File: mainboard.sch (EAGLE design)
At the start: 128 parts, among them X1 FH12-24S-0.5SH, X3 87438-02

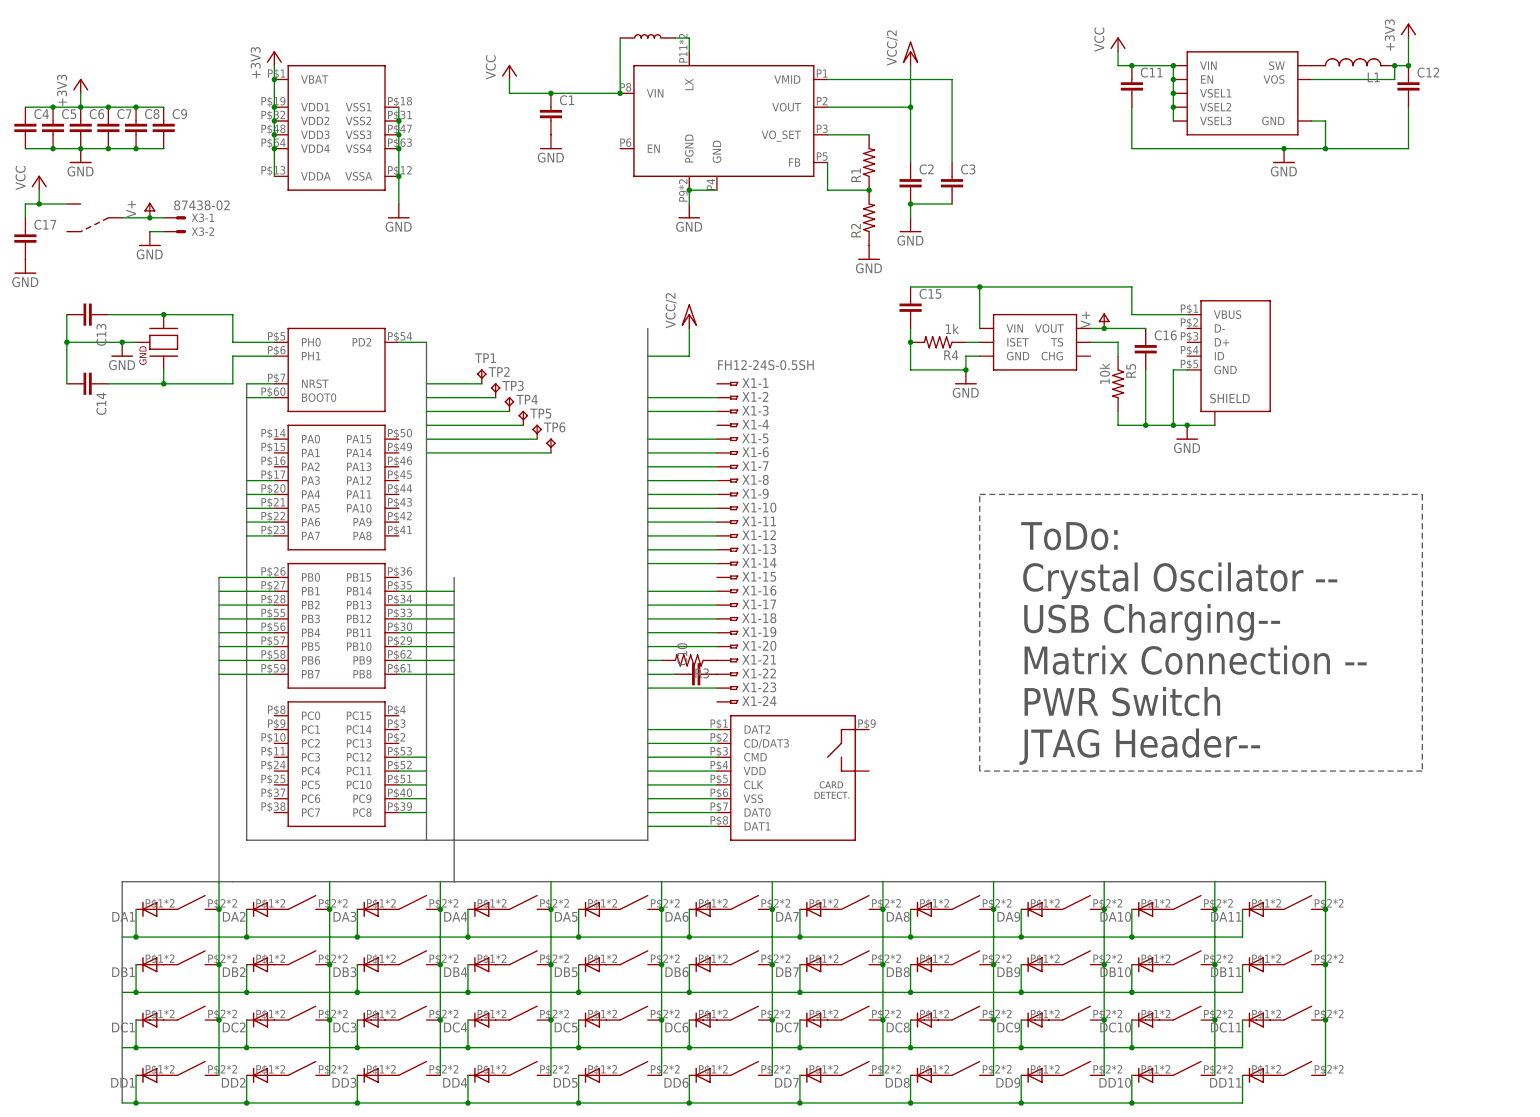
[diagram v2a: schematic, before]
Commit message: Fixed Issues/New features
Battery level sensing
microSD card sensing

Fixed issues:
Boot0 pulldown resistor
NRST pullup resistor
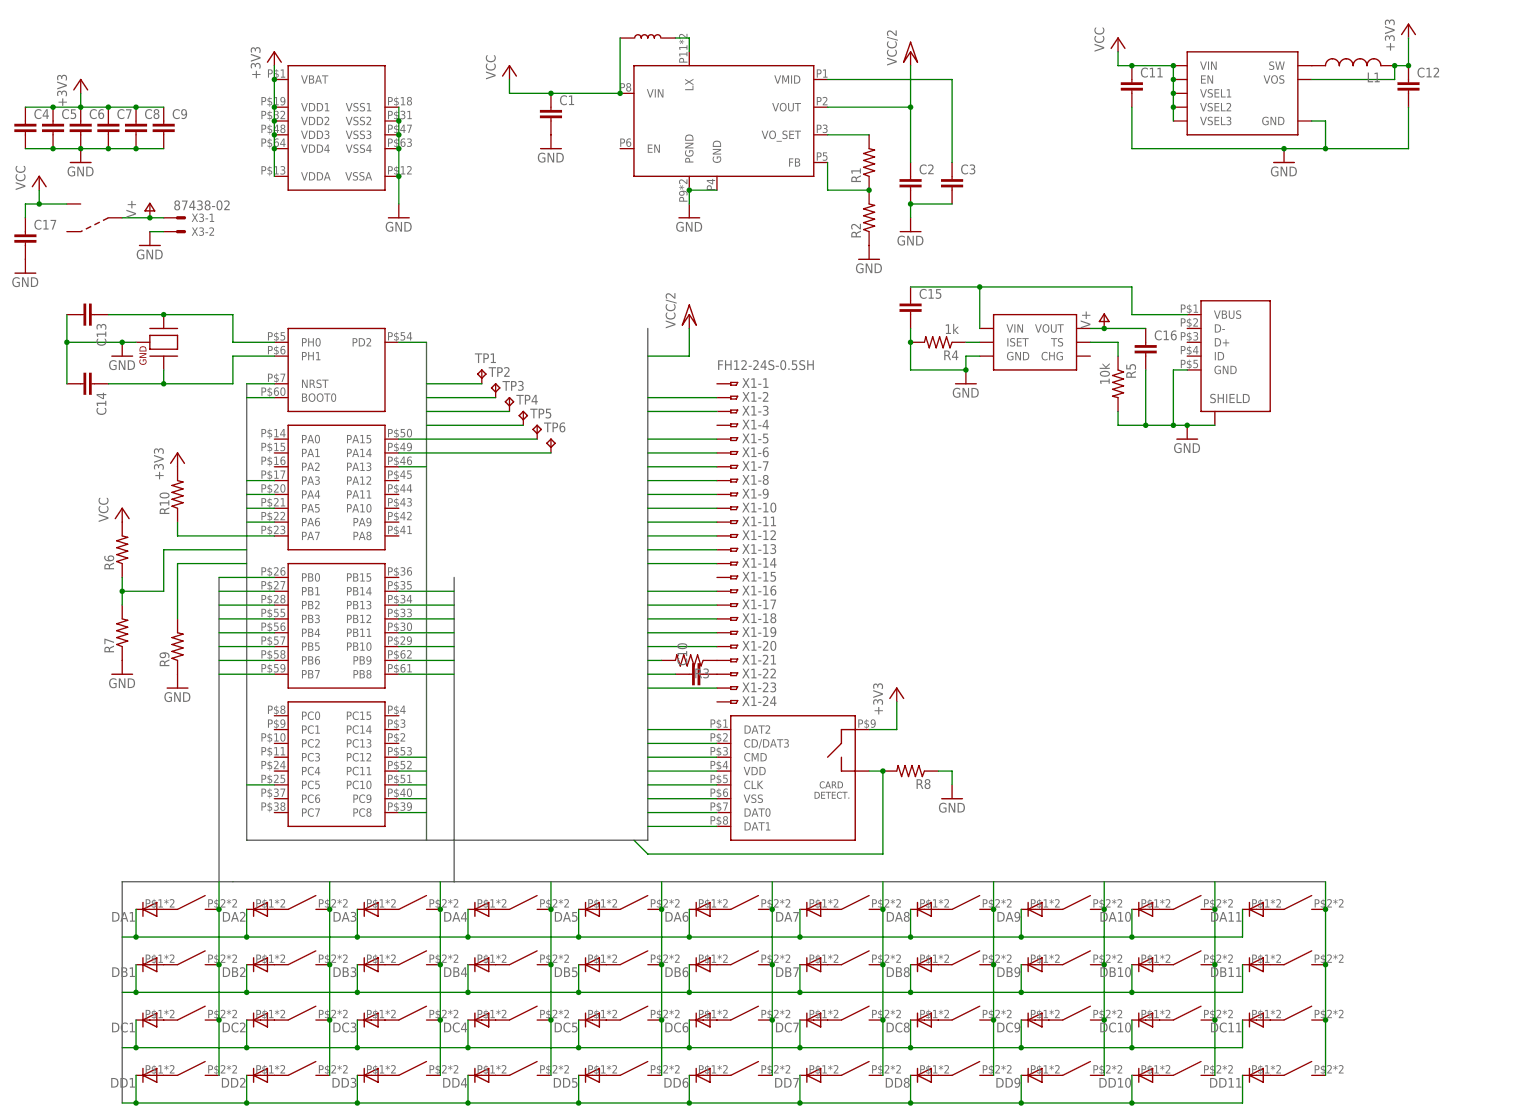
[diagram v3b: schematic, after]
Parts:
- added R10, R6, R7, R8, R9: (no value), resistor:R-US_R0402
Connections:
- new net BAT_SENS: R6.1, R7.2, U$1G$4.PC5
- new net SD_SWITCH: R8.2, U$1G$2.PA15, U$2.P$10
- net +3V3: now also R10.2, U$2.P$9
- net BOOT0: now also R9.2
- net GND: now also R7.1, R8.1, R9.1
- net NRST: now also R10.1
- net PA13: now also U$1G$2.PA13
- net PA14: now also U$1G$2.PA14
- net VCC: now also R6.2
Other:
- note removed: "ToDo: Crystal Oscilator -- USB Charging-- Matrix Connection -- PWR Switch JTAG Header--"
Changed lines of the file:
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@@
 <part name="C17" library="eagle-ltspice" deviceset="C" device="C1206"/>
 <part name="GND12" library="supply1" deviceset="GND" device=""/>
+<part name="R6" library="resistor" deviceset="R-US_" device="R0402"/>
+<part name="R7" library="resistor" deviceset="R-US_" device="R0402"/>
+<part name="GND13" library="supply1" deviceset="GND" device=""/>
+<part name="P+6" library="supply1" deviceset="VCC" device=""/>
+<part name="+3V4" library="supply1" deviceset="+3V3" device=""/>
+<part name="R8" library="resistor" deviceset="R-US_" device="R0402"/>
+<part name="GND14" library="supply1" deviceset="GND" device=""/>
+<part name="R9" library="resistor" deviceset="R-US_" device="R0402"/>
+<part name="GND15" library="supply1" deviceset="GND" device=""/>
+<part name="R10" library="resistor" deviceset="R-US_" device="R0402"/>
+<part name="+3V5" library="supply1" deviceset="+3V3" device=""/>
 </parts>
 <sheets>
 <sheet>
 <plain>
-<text x="170.18" y="66.04" size="5.08" layer="97">ToDo:
-Crystal Oscilator --
-USB Charging--
-Matrix Connection --
-PWR Switch
-JTAG Header--</text>
-<wire x1="162.56" y1="114.3" x2="243.84" y2="114.3" width="0.1524" layer="97" style="shortdash"/>
-<wire x1="243.84" y1="114.3" x2="243.84" y2="63.5" width="0.1524" layer="97" style="shortdash"/>
-<wire x1="243.84" y1="63.5" x2="162.56" y2="63.5" width="0.1524" layer="97" style="shortdash"/>
-<wire x1="162.56" y1="63.5" x2="162.56" y2="114.3" width="0.1524" layer="97" style="shortdash"/>
 </plain>
 <instances>
@@
 <instance part="C17" gate="G$1" x="-12.7" y="162.56"/>
 <instance part="GND12" gate="1" x="-12.7" y="154.94"/>
+<instance part="R6" gate="G$1" x="5.08" y="104.14" rot="R90"/>
+<instance part="R7" gate="G$1" x="5.08" y="88.9" rot="R90"/>
+<instance part="GND13" gate="1" x="5.08" y="81.28"/>
+<instance part="P+6" gate="VCC" x="5.08" y="111.76"/>
+<instance part="+3V4" gate="G$1" x="147.32" y="78.74"/>
+<instance part="R8" gate="G$1" x="149.86" y="63.5" rot="R180"/>
+<instance part="GND14" gate="1" x="157.48" y="58.42"/>
+<instance part="R9" gate="G$1" x="15.24" y="86.36" rot="R90"/>
+<instance part="GND15" gate="1" x="15.24" y="78.74"/>
+<instance part="R10" gate="G$1" x="15.24" y="114.3" rot="R90"/>
+<instance part="+3V5" gate="G$1" x="15.24" y="121.92"/>
 </instances>
 <busses>
-<bus name="SD_CLK,SD_CMD,SD_DAT[0..3],+3V3,GND,SPI_CS,SPI_SCK,SPI_MISO,SPI_MOSI,VCC/2,PA[0..15],PB[0..15],PC[0..15],BOOT0,NRST">
+<bus name="SD_CLK,SD_CMD,SD_DAT[0..3],+3V3,GND,SPI_CS,SPI_SCK,SPI_MISO,SPI_MOSI,VCC/2,PA[0..15],PB[0..15],PC[0..15],BOOT0,NRST,BAT_SENS,SD_SWITCH">
 <segment>
 <wire x1="27.94" y1="134.62" x2="27.94" y2="50.8" width="0.762" layer="92"/>
@@
 <pinref part="C17" gate="G$1" pin="2"/>
 <pinref part="GND12" gate="1" pin="GND"/>
+</segment>
+<segment>
+<pinref part="R7" gate="G$1" pin="1"/>
+<pinref part="GND13" gate="1" pin="GND"/>
+</segment>
+<segment>
+<pinref part="R8" gate="G$1" pin="1"/>
+<pinref part="GND14" gate="1" pin="GND"/>
+<wire x1="154.94" y1="63.5" x2="157.48" y2="63.5" width="0.1524" layer="91"/>
+<wire x1="157.48" y1="63.5" x2="157.48" y2="60.96" width="0.1524" layer="91"/>
+</segment>
+<segment>
+<pinref part="R9" gate="G$1" pin="1"/>
+<pinref part="GND15" gate="1" pin="GND"/>
 </segment>
 </net>
@@
 <pinref part="TP1" gate="G$1" pin="TP"/>
 <wire x1="71.12" y1="134.62" x2="60.96" y2="134.62" width="0.1524" layer="91"/>
+</segment>
+<segment>
+<pinref part="U$2" gate="G$1" pin="P$9"/>
+<pinref part="+3V4" gate="G$1" pin="+3V3"/>
+<wire x1="142.24" y1="71.12" x2="147.32" y2="71.12" width="0.1524" layer="91"/>
+<wire x1="147.32" y1="71.12" x2="147.32" y2="76.2" width="0.1524" layer="91"/>
+</segment>
+<segment>
+<pinref part="R10" gate="G$1" pin="2"/>
+<pinref part="+3V5" gate="G$1" pin="+3V3"/>
 </segment>
 </net>
@@
 <wire x1="-10.16" y1="167.64" x2="-5.08" y2="167.64" width="0.1524" layer="91"/>
 <junction x="-10.16" y="167.64"/>
+</segment>
+<segment>
+<pinref part="R6" gate="G$1" pin="2"/>
+<pinref part="P+6" gate="VCC" pin="VCC"/>
 </segment>
 </net>
@@
 <wire x1="73.66" y1="132.08" x2="60.96" y2="132.08" width="0.1524" layer="91"/>
 </segment>
+<segment>
+<pinref part="U$1" gate="G$2" pin="PA13"/>
+<wire x1="55.88" y1="119.38" x2="60.96" y2="119.38" width="0.1524" layer="91"/>
+</segment>
 </net>
 <net name="PA14" class="0">
@@
 <wire x1="76.2" y1="129.54" x2="60.96" y2="129.54" width="0.1524" layer="91"/>
 </segment>
+<segment>
+<pinref part="U$1" gate="G$2" pin="PA14"/>
+<wire x1="55.88" y1="121.92" x2="60.96" y2="121.92" width="0.1524" layer="91"/>
+</segment>
 </net>
 <net name="BOOT0" class="0">
@@
 <wire x1="81.28" y1="124.46" x2="60.96" y2="124.46" width="0.1524" layer="91"/>
 </segment>
+<segment>
+<pinref part="R9" gate="G$1" pin="2"/>
+<wire x1="15.24" y1="91.44" x2="15.24" y2="101.6" width="0.1524" layer="91"/>
+<wire x1="15.24" y1="101.6" x2="27.94" y2="101.6" width="0.1524" layer="91"/>
+</segment>
 </net>
 <net name="NRST" class="0">
@@
 <pinref part="TP6" gate="G$1" pin="TP"/>
 <wire x1="83.82" y1="121.92" x2="60.96" y2="121.92" width="0.1524" layer="91"/>
+</segment>
+<segment>
+<pinref part="R10" gate="G$1" pin="1"/>
+<wire x1="15.24" y1="109.22" x2="15.24" y2="106.68" width="0.1524" layer="91"/>
+<wire x1="15.24" y1="106.68" x2="27.94" y2="106.68" width="0.1524" layer="91"/>
 </segment>
 </net>
@@
 </segment>
 </net>
+<net name="BAT_SENS" class="0">
+<segment>
+<pinref part="U$1" gate="G$4" pin="PC5"/>
+<wire x1="33.02" y1="60.96" x2="27.94" y2="60.96" width="0.1524" layer="91"/>
+</segment>
+<segment>
+<wire x1="27.94" y1="104.14" x2="12.7" y2="104.14" width="0.1524" layer="91"/>
+<wire x1="12.7" y1="104.14" x2="12.7" y2="96.52" width="0.1524" layer="91"/>
+<pinref part="R6" gate="G$1" pin="1"/>
+<pinref part="R7" gate="G$1" pin="2"/>
+<wire x1="5.08" y1="99.06" x2="5.08" y2="96.52" width="0.1524" layer="91"/>
+<wire x1="5.08" y1="96.52" x2="5.08" y2="93.98" width="0.1524" layer="91"/>
+<wire x1="12.7" y1="96.52" x2="5.08" y2="96.52" width="0.1524" layer="91"/>
+<junction x="5.08" y="96.52"/>
+</segment>
+</net>
+<net name="SD_SWITCH" class="0">
+<segment>
+<pinref part="U$1" gate="G$2" pin="PA15"/>
+<wire x1="55.88" y1="124.46" x2="60.96" y2="124.46" width="0.1524" layer="91"/>
+</segment>
+<segment>
+<wire x1="101.6" y1="48.26" x2="144.78" y2="48.26" width="0.1524" layer="91"/>
+<wire x1="144.78" y1="48.26" x2="144.78" y2="63.5" width="0.1524" layer="91"/>
+<pinref part="U$2" gate="G$1" pin="P$10"/>
+<wire x1="144.78" y1="63.5" x2="142.24" y2="63.5" width="0.1524" layer="91"/>
+<pinref part="R8" gate="G$1" pin="2"/>
+<junction x="144.78" y="63.5"/>
+<wire x1="99.06" y1="50.8" x2="101.6" y2="48.26" width="0.1524" layer="91"/>
+</segment>
+</net>

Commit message: Minor Stetic Modifications
DIN-A4 frame in schematic and relocation.
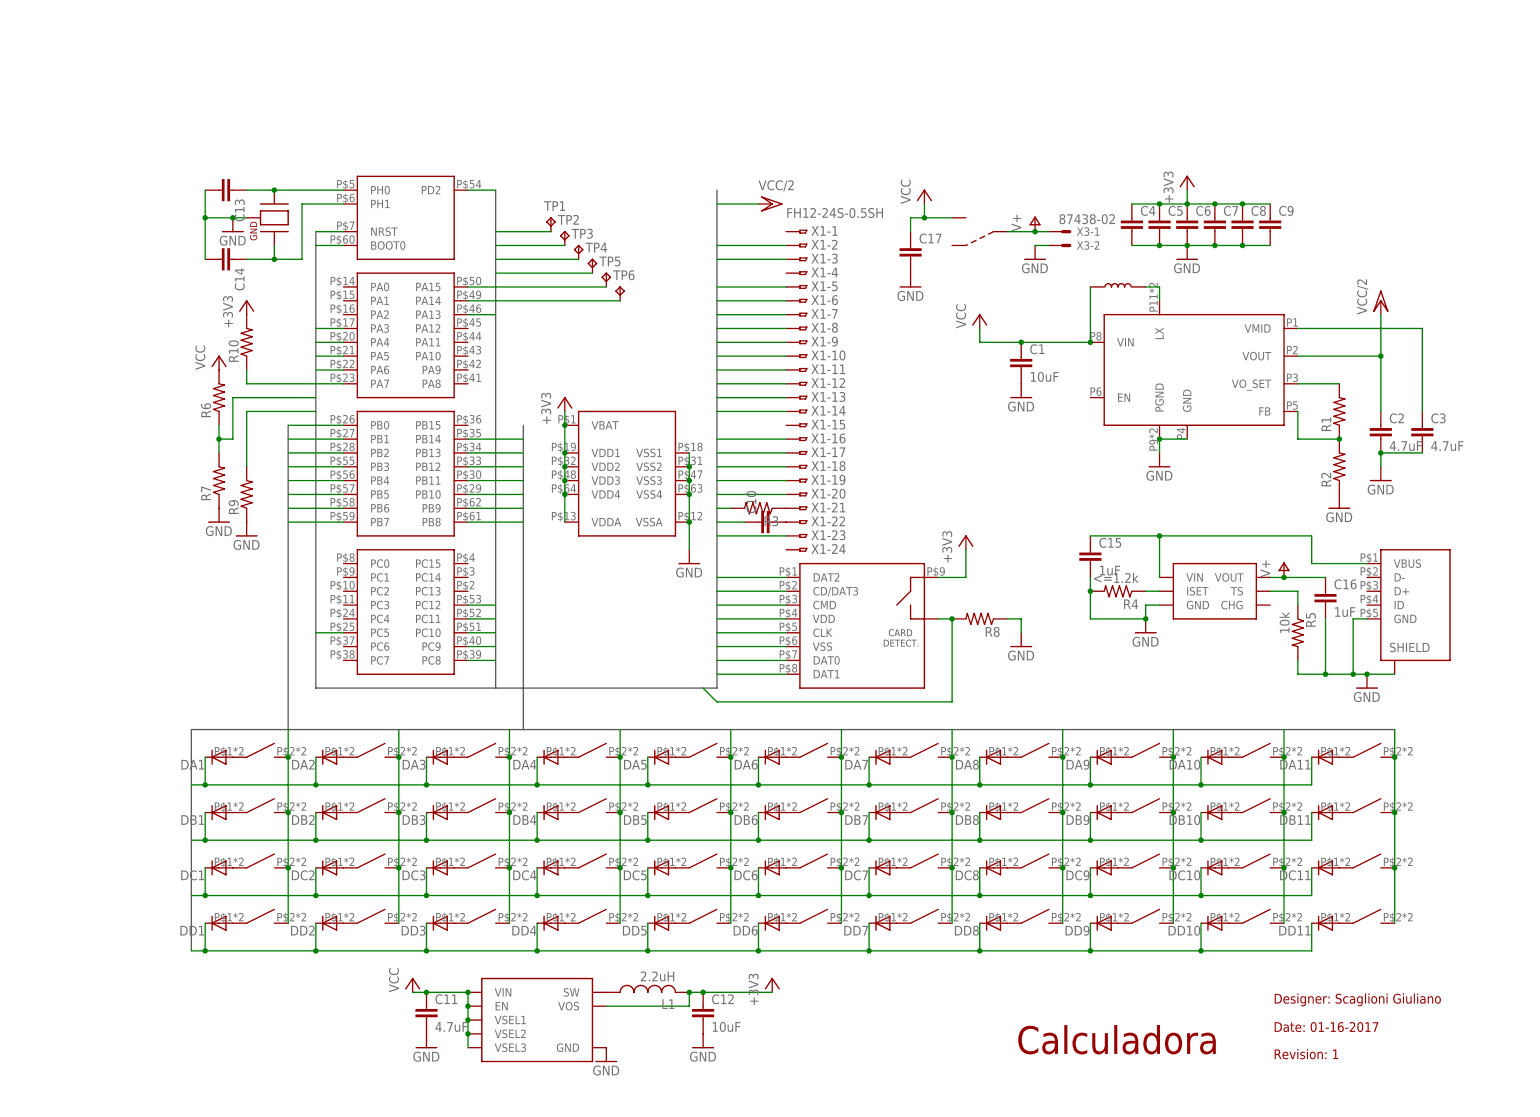
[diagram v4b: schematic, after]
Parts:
- C1, C12: value (none) -> 10uF
- C11, C2, C3: value (none) -> 4.7uF
- C15, C16: value (none) -> 1uF
- L1: value (none) -> 2.2uH
- R4: value 1k -> <=1.2k
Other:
- note added: "Calculadora"
- note added: "Date: 01-16-2017"
- note added: "Designer: Scaglioni Giuliano"
- note added: "Revision: 1"
- moved on the sheet: C1, C10, C11, C12, C13, C14, C15, C16, C17, C2, C3, C4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
